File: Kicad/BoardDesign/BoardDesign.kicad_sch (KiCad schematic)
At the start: 1 part, among them U1 ESP32-C3-MINI-1

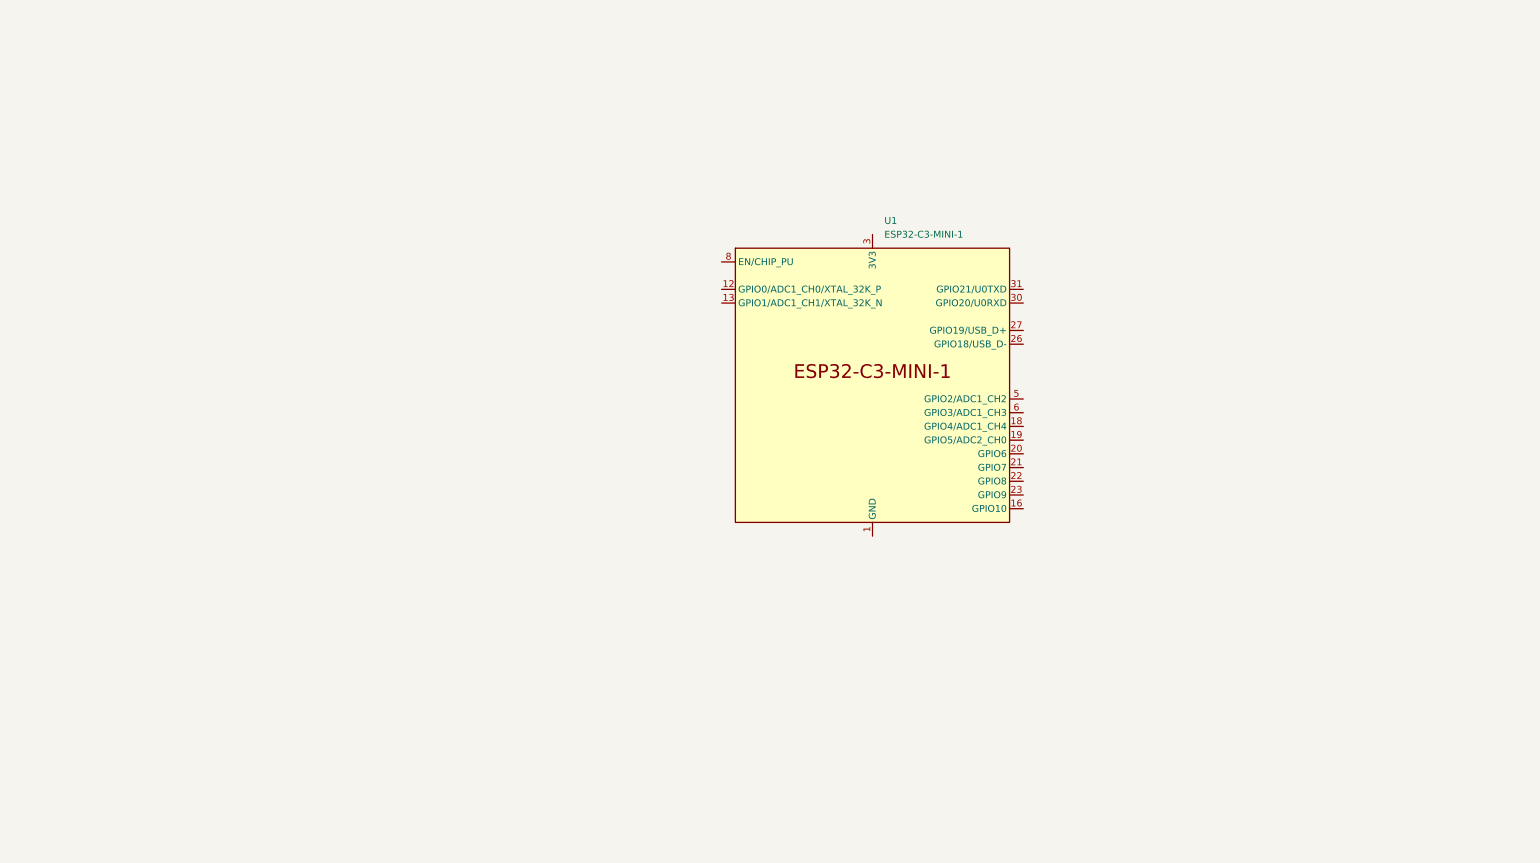
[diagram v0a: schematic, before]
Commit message: Todos los componentes
Falta conectar el hx717 y comprobar valores de resistencias, condensadores, etc.
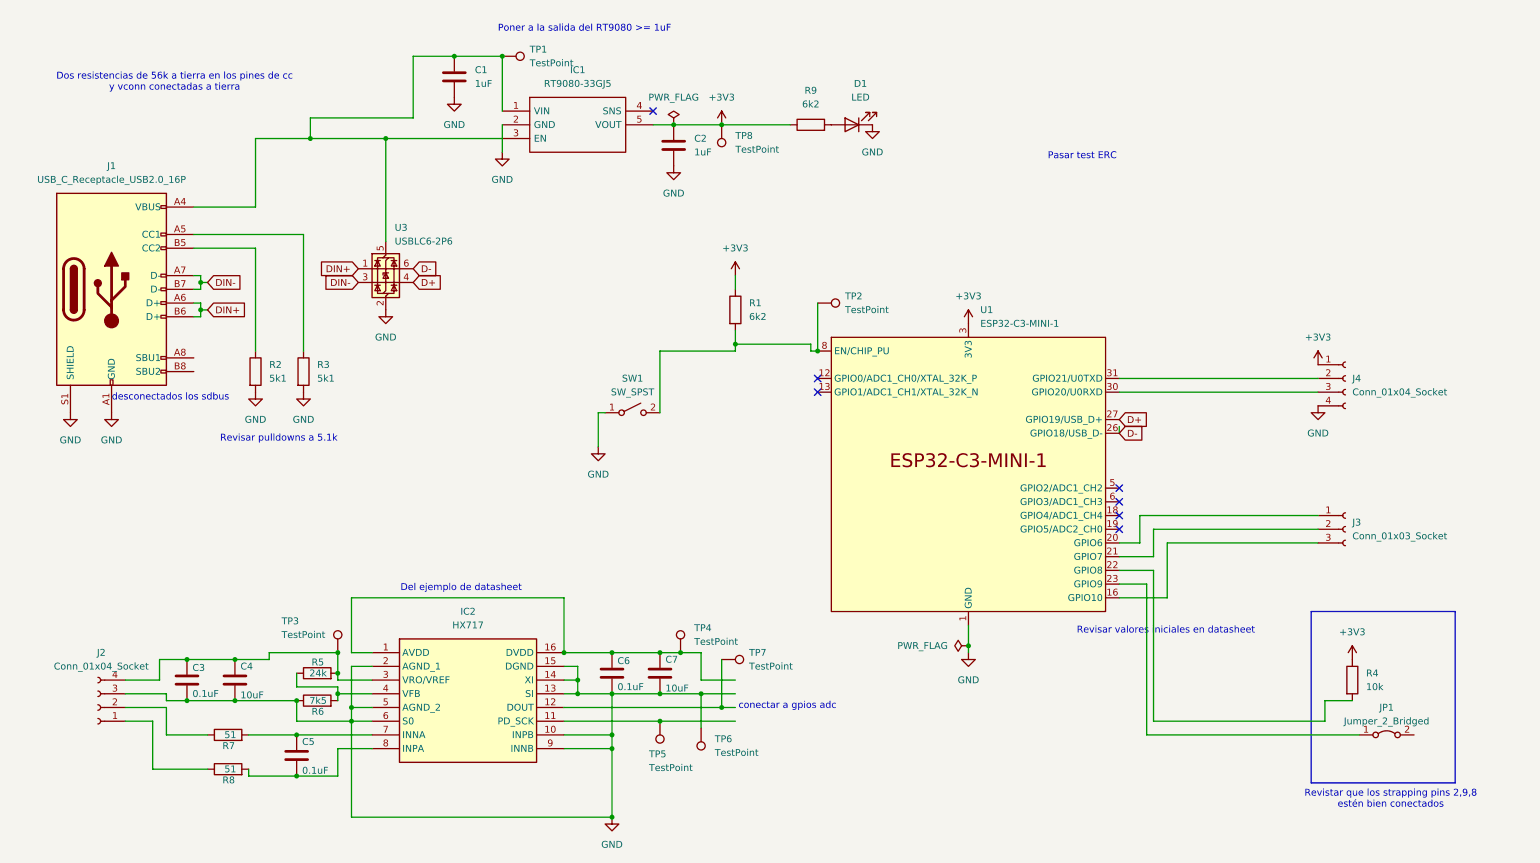
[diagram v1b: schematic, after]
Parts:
- added C1, C2: 1uF, symbol Device:C
- added C3, C5, C6: 0.1uF, symbol Device:C
- added C4, C7: 10uF, symbol Device:C
- added D1: LED, symbol Device:LED
- added IC1: RT9080-33GJ5, SOT94P280X100-5N, symbol esp:RT9080-33GJ5
- added IC2: HX717, SOIC127P600X160-16N, symbol HX717:HX717
- added J1: USB_C_Receptacle_USB2.0_16P, symbol Connector:USB_C_Receptacle_USB2.0_16P
- added J2: Conn_01x04_Socket, symbol Connector:Conn_01x04_Socket
- added J3: Conn_01x03_Socket, symbol Connector:Conn_01x03_Socket
- added J4: Conn_01x04_Socket, Connector_PinHeader_1.00mm:PinHeader_1x04_P1.00mm_Vertical, symbol Connector:Conn_01x04_Socket
- added JP1: Jumper_2_Bridged, Connector_PinHeader_1.00mm:PinHeader_1x02_P1.00mm_Vertical, symbol Jumper:Jumper_2_Bridged
- added R1, R9: 6k2, Capacitor_SMD:C_0603_1608Metric, symbol Device:R
- added R2, R3: 5k1, Capacitor_SMD:C_0402_1005Metric, symbol Device:R
- added R4: 10k, symbol Device:R
- added R5: 24k, Capacitor_SMD:C_0603_1608Metric, symbol Device:R
- added R6: 7k5, Capacitor_SMD:C_0603_1608Metric, symbol Device:R
- added R7, R8: 51, Capacitor_SMD:C_0603_1608Metric, symbol Device:R
- added SW1: SW_SPST, AAA_Footprints:TS1187ABAB, symbol Switch:SW_SPST
- added TP1, TP2, TP3, TP4, TP5, TP6, TP7, TP8: TestPoint, symbol Connector:TestPoint
- added U3: USBLC6-2P6, Package_TO_SOT_SMD:SOT-666, symbol Power_Protection:USBLC6-2P6
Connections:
- net GND: now reaches U1.1 (GND), U1.11 (GND), U1.14 (GND), U1.2 (GND), U1.36 (GND), U1.37 (GND), U1.38 (GND), U1.39 (GND), U1.40 (GND), U1.41 (GND), U1.42 (GND), U1.43 (GND), U1.44 (GND), U1.45 (GND), U1.46 (GND), U1.47 (GND), U1.48 (GND), U1.49 (GND), U1.50 (GND), U1.51 (GND), U1.52 (GND), U1.53 (GND)
- net GND: now also C1.2, C2.2, C3.2, C4.2, C6.2, C7.2, D1.1 (K), IC1.2 (GND), IC2.10 (INPB), IC2.13 (SI), IC2.14 (XI), IC2.15 (DGND), IC2.2 (AGND_1), IC2.5 (AGND_2), IC2.6 (S0), IC2.9 (INNB), J1.A1 (GND), J1.A12 (GND), J1.B1 (GND), J1.B12 (GND), J1.S1 (SHIELD), J2.3 (Pin_3), J4.4 (Pin_4), R2.2, R3.2, R6.1, SW1.1 (A), TP6.1, U3.2 (GND)
- net at U1.16 (GPIO10): now also J3.3 (Pin_3)
- net at U1.20 (GPIO6): now also J3.1 (Pin_1)
- net at U1.21 (GPIO7): now also J3.2 (Pin_2)
- net at U1.22 (GPIO8): now also R4.2
- net at U1.23 (GPIO9): now also JP1.1 (A)
- net D-: now reaches U1.26 (GPIO18/USB_D-)
- net D-: now also U3.6 (I/O1)
- net D+: now reaches U1.27 (GPIO19/USB_D+)
- net D+: now also U3.4 (I/O2)
- net +3V3: now reaches U1.3 (3V3)
- net +3V3: now also C2.1, IC1.5 (VOUT), J4.1 (Pin_1), R1.1, R4.1, R9.1, TP8.1
- net at U1.30 (GPIO20/U0RXD): now also J4.3 (Pin_3)
- net at U1.31 (GPIO21/U0TXD): now also J4.2 (Pin_2)
- net at U1.8 (EN/CHIP_PU): now also R1.2, SW1.2 (B), TP2.1
- new net: D1.2 (A), R9.2
- new net: J2.1 (Pin_1), R8.1
- new net: C5.2, IC2.8 (INPA), R8.2
- new net: C1.1, IC1.1 (VIN), IC1.3 (EN), J1.A4 (VBUS), J1.A9 (VBUS), J1.B4 (VBUS), J1.B9 (VBUS), TP1.1, U3.5 (VBUS)
- new net: C6.1, C7.1, IC2.1 (AVDD), IC2.16 (DVDD), TP4.1
- new net: IC2.11 (PD_SCK), TP5.1
- new net: IC2.12 (DOUT), TP7.1
- new net: C3.1, C4.1, IC2.3 (VRO/VREF), J2.4 (Pin_4), R5.2, TP3.1
- new net: IC2.4 (VFB), R5.1, R6.2
- new net: C5.1, IC2.7 (INNA), R7.2
- new net: J1.B5 (CC2), R2.1
- new net: J1.A5 (CC1), R3.1
- new net: J2.2 (Pin_2), R7.1
- new net DIN+: J1.A6 (D+), J1.B6 (D+), U3.1 (I/O1)
- new net DIN-: J1.A7 (D-), J1.B7 (D-), U3.3 (I/O2)
- no-connect marks 0 -> 7
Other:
- note added: "Del ejemplo de datasheet"
- note added: "Dos resistencias de 56k a tierra en los pines de cc y vconn conectadas a tierra"
- note added: "Pasar test ERC"
- note added: "Poner a la salida del RT9080 >= 1uF"
- note added: "Revisar pulldowns a 5.1k"
- note added: "Revisar valores iniciales en datasheet"
- note added: "Revistar que los strapping pins 2,9,8 estén bien conectados"
- note added: "conectar a gpios adc"
- note added: "desconectados los sdbus"
- moved on the sheet: U1

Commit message: Cambios con Dani
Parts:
- removed C1: 1uF, symbol Device:C
- removed U3: USBLC6-2P6, Package_TO_SOT_SMD:SOT-666, symbol Power_Protection:USBLC6-2P6
- added C4: 1uF, symbol Device:C
- added R10: 10k, symbol Device:R
- added U1: USBLC6-2P6, Package_TO_SOT_SMD:SOT-666, symbol Power_Protection:USBLC6-2P6
- renumbered C3 to C1, C4 to C2, C5 to C3, C6 to C5, C7 to C6, C2 to C7, IC2 to IC1, IC1 to IC2, J2 to J1, J1 to J2, J4 to J3, J3 to J4, R7 to R1, R8 to R2, R2 to R3, R3 to R4, R1 to R7, R9 to R8, R4 to R9, TP3 to TP1, TP1 to TP2, TP5 to TP3, TP8 to TP5, TP7 to TP6, TP6 to TP7, TP2 to TP8, U1 to U2
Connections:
- net +3V3: now also C5.1, C6.1, IC1.1 (AVDD), IC1.16 (DVDD), TP4.1
- net D+: now also U1.4 (I/O2)
- net D-: now also U1.6 (I/O1)
- net DIN+: now also U1.1 (I/O1)
- net DIN-: now also U1.3 (I/O2)
- net GND: now also C4.2, R10.2, U1.2 (GND); no longer IC1.13 (SI), IC1.6 (S0), TP7.1
- net at IC2.1 (VIN), IC2.3 (EN), J2.A4 (VBUS)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: now also C4.1, U1.5 (VBUS)
- net PD_SCK: now reaches IC1.11 (PD_SCK), TP3.1
- net PD_SCK: now also U2.19 (GPIO5/ADC2_CH0)
- net DOUT: now reaches IC1.12 (DOUT), TP6.1
- net DOUT: now also U2.18 (GPIO4/ADC1_CH4)
- net Del boot mode de la documentación: now reaches JP1.1 (A), U2.23 (GPIO9)
- net S0: now reaches U2.5 (GPIO2/ADC1_CH2)
- net S0: now also IC1.6 (S0)
- net S1: now reaches U2.6 (GPIO3/ADC1_CH3)
- net S1: now also IC1.13 (SI), TP7.1
- net at JP1.2 (B): now also R10.1
- no-connect marks 7 -> 5
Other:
- note removed: "Revistar que los strapping pins 2,9,8 estén bien conectados"
- note removed: "conectar a gpios adc"
- moved on the sheet: D1, J4, R8, TP6, TP7

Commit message: "Inicio rutado kicad"
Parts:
- removed IC2: RT9080-33GJ5, SOT94P280X100-5N, symbol esp:RT9080-33GJ5
- added IC2: RT9080-33GJ5, SOT94P280X100-5N, symbol RT9080-33GJ5:RT9080-33GJ5
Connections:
- net +3V3: now also IC2.5 (VOUT)
- net GND: now also IC2.2 (GND)
- net at C4.1, J2.A4 (VBUS), J2.A9 (VBUS)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: now also IC2.1 (VIN), IC2.3 (EN)
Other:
- note added: "De la datasheet con sns desconectado vout da 3,3v"
- note added: "Dos resistencias de 5k1 a tierra en los pines de cc y vconn conectadas a tierra"
- note removed: "Dos resistencias de 56k a tierra en los pines de cc y vconn conectadas a tierra"
- note removed: "Pasar test ERC"
- note removed: "Revisar pulldowns a 5.1k"
- note removed: "Revisar valores iniciales en datasheet"
- moved on the sheet: D1, TP2

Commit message: Kicad corregido
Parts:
- removed J4: Conn_01x03_Socket, symbol Connector:Conn_01x03_Socket
- removed JP1: Jumper_2_Bridged, Connector_PinHeader_1.00mm:PinHeader_1x02_P1.00mm_Vertical, symbol Jumper:Jumper_2_Bridged
- added C8: 0.1uF, Capacitor_SMD:C_0603_1608Metric, symbol Device:C
- added D2: LED, LED_SMD:LED_0603_1608Metric, symbol Device:LED
- added J4: Conn_01x04_Socket, Connector_PinHeader_2.54mm:PinHeader_1x04_P2.54mm_Vertical, symbol Connector:Conn_01x04_Socket
- added SW2, SW3, SW4: SW_SPST, AAA_Footprints:TS1187ABAB, symbol Switch:SW_SPST
- C1, C2, C3, C5, C6: footprint (none) -> Capacitor_SMD:C_0603_1608Metric
- C4, C7: value 1uF -> 10uF; footprint (none) -> Capacitor_SMD:C_0603_1608Metric
- D1: footprint (none) -> LED_SMD:LED_0603_1608Metric
- J1: footprint (none) -> Connector_PinHeader_2.54mm:PinHeader_1x04_P2.54mm_Vertical
- J2: footprint (none) -> Connector_USB:USB_C_Receptacle_GCT_USB4105-xx-A_16P_TopMnt_Horizontal
- J3: footprint Connector_PinHeader_1.00mm:PinHeader_1x04_P1.00mm_Vertical -> Connector_PinHeader_2.54mm:PinHeader_1x04_P2.54mm_Vertical
- R10: footprint (none) -> Capacitor_SMD:C_0603_1608Metric; JLCPCB (none) -> C4260
- R3, R4: footprint Capacitor_SMD:C_0402_1005Metric -> Capacitor_SMD:C_0603_1608Metric
- R5: value 24k -> 47K
- R6: value 7k5 -> 27K
- R7: value 6k2 -> 10k
- R8: value 6k2 -> 5k1
- R9: value 10k -> 5k1; footprint (none) -> Capacitor_SMD:C_0603_1608Metric; JLCPCB (none) -> C4260
- TP1, TP2, TP3, TP4, TP5, TP6, TP7, TP8: footprint (none) -> TestPoint:TestPoint_Pad_D1.5mm
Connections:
- net +3V3: now also R10.1, J4.1 (Pin_1); no longer R9.1
- net D+: now also U1.6 (I/O1); no longer U1.4 (I/O2)
- net D-: now also U1.4 (I/O2); no longer U1.6 (I/O1)
- net DOUT: now also U2.20 (GPIO6); no longer U2.18 (GPIO4/ADC1_CH4)
- net GND: now also C8.2, D2.1 (K), J4.4 (Pin_4), SW2.1 (A), SW3.1 (A), SW4.1 (A); no longer R10.2
- net PD_SCK: now also U2.21 (GPIO7); no longer U2.19 (GPIO5/ADC2_CH0)
- net S0: now also U2.18 (GPIO4/ADC1_CH4); no longer U2.5 (GPIO2/ADC1_CH2)
- net S1: now also U2.19 (GPIO5/ADC2_CH0); no longer U2.6 (GPIO3/ADC1_CH3)
- net at U2.22 (GPIO8): now also R10.2; no longer R9.2
- net at U2.16 (GPIO10): now also R9.1
- net at R7.2, SW1.2 (B), TP8.1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: now also C8.1
- net at U2.12 (GPIO0/ADC1_CH0/XTAL_32K_P): now also SW2.2 (B)
- net at U2.13 (GPIO1/ADC1_CH1/XTAL_32K_N): now also SW3.2 (B)
- net Del boot mode de la documentación: no longer names the net of U2.23 (GPIO9)
- net Del boot mode de la documentación: now also SW4.2 (B)
- new net: J4.2 (Pin_2), U2.5 (GPIO2/ADC1_CH2)
- new net: J4.3 (Pin_3), U2.6 (GPIO3/ADC1_CH3)
- new net: D2.2 (A), R9.2
- no-connect marks 5 -> 3
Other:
- note added: "Datasheet del USBLC6-2 (https://octopart.com/datasheet/ usblc6-2p6-stmicroelectronics-347175) Para conexiones"
- note added: "Del datasheet del hx717: VRO=1.11*(R1+R2)/R2. VRO should be set at least 200mV lower than AVDD."
- note added: "Dos resistencias de 5k1 a tierra en los pines de cc y vconn conectadas a tierra (Protocolo USB para 500mA)"
- note added: "Figura 7 datasheet ejemplo de uso"
- note added: "Figura 7 datasheet ejemplo de uso. Posibilidad de arrancar en modo boot"
- note added: "SBU no es necesario"
- note added: "UART"
- note removed: "Del ejemplo de datasheet"
- note removed: "Dos resistencias de 5k1 a tierra en los pines de cc y vconn conectadas a tierra"
- note removed: "desconectados los sdbus"
- moved on the sheet: SW1
